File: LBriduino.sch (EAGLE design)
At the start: 13 parts, among them J1 105017-0001

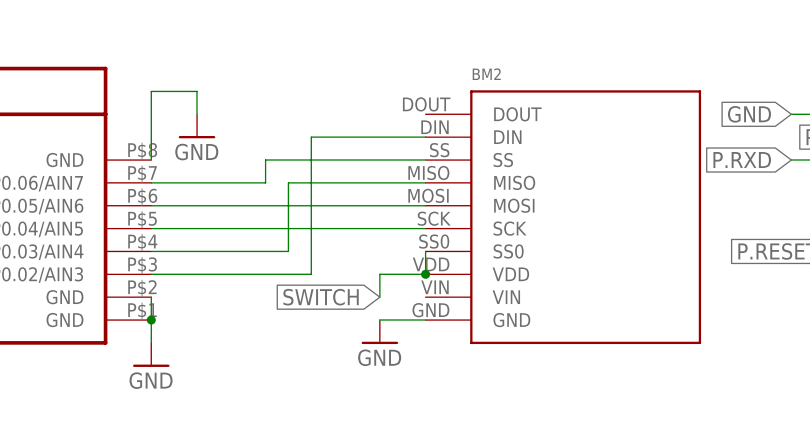
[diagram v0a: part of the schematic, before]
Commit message: reverted BM019 input to VIN
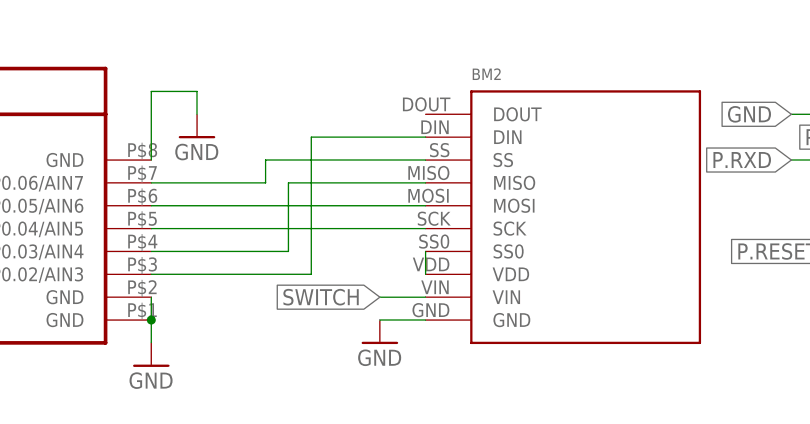
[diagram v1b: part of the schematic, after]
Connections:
- new net N$5: BM2.SS0, BM2.VDD
- net SWITCH: now also BM2.VIN; no longer BM2.SS0, BM2.VDD
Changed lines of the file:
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@@
 <segment>
 <label x="53.34" y="0" size="1.778" layer="95" rot="MR0" xref="yes"/>
-<pinref part="BM2" gate="G$1" pin="VDD"/>
-<pinref part="BM2" gate="G$1" pin="SS0"/>
-<wire x1="58.42" y1="2.54" x2="58.42" y2="5.08" width="0.1524" layer="91"/>
-<wire x1="58.42" y1="2.54" x2="53.34" y2="2.54" width="0.1524" layer="91"/>
-<junction x="58.42" y="2.54"/>
-<wire x1="53.34" y1="2.54" x2="53.34" y2="0" width="0.1524" layer="91"/>
+<pinref part="BM2" gate="G$1" pin="VIN"/>
+<wire x1="58.42" y1="0" x2="53.34" y2="0" width="0.1524" layer="91"/>
 </segment>
 <segment>
@@
 </segment>
 </net>
+<net name="N$5" class="0">
+<segment>
+<pinref part="BM2" gate="G$1" pin="SS0"/>
+<pinref part="BM2" gate="G$1" pin="VDD"/>
+<wire x1="58.42" y1="2.54" x2="58.42" y2="5.08" width="0.1524" layer="91"/>
+</segment>
+</net>
